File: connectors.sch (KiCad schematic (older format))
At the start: 29 parts, among them J10 Servo3, J11 Servo4, J12 Servo5, J13 CAN, J14 Servo6, J15 Servo7, J16 Servo8, J8 Servo1, J9 Servo2, U3 LP38693-5.0, U4 TXB0108DQSR, U5 MCP2551

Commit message: Final changes in schema
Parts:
- added C16: 10uF, symbol Device:CP
- C13: renamed from C15; value 100uF -> 10uF
- renumbered C16 to C14, C17 to C15, C18 to C17, C19 to C18, C20 to C19, C21 to C20, C22 to C21, C23 to C22, C24 to C23, C25 to C24, C26 to C25, C27 to C26, C28 to C27
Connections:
- net GND: now also C16.2
- net VCCOUT: now also C16.1
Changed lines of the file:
@@
 encoding utf-8
 Sheet 2 3
-Title ""
-Date ""
-Rev ""
-Comp ""
-Comment1 ""
+Title "SX1280 based RC receiver"
+Date "2019-02-25"
+Rev "1"
+Comp "bodrico.com"
+Comment1 "Designed by bodri@bodrico.com"
 Comment2 ""
 Comment3 ""
@@
 	8375 2150 8225 2150
 $Comp
-L Device:C C16
+L Device:C C14
 U 1 1 5C78CA1B
 P 6550 2250
-F 0 "C16" H 6665 2296 50  0000 L CNN
+F 0 "C14" H 6665 2296 50  0000 L CNN
 F 1 "1uF" H 6665 2205 50  0000 L CNN
 F 2 "" H 6588 2100 50  0001 C CNN
@@
 $EndComp
 $Comp
-L Device:C C17
+L Device:C C15
 U 1 1 5C78CA91
 P 8375 2300
-F 0 "C17" H 8490 2346 50  0000 L CNN
+F 0 "C15" H 8490 2346 50  0000 L CNN
 F 1 "1uF" H 8490 2255 50  0000 L CNN
 F 2 "" H 8413 2150 50  0001 C CNN
@@
 	7825 2500 7825 2450
 Wire Wire Line
-	8375 2050 8675 2050
+	8375 2050 8750 2050
 Connection ~ 8375 2050
-Text Label 8400 2050 0    50   ~ 0
+Text Label 8950 2050 0    50   ~ 0
 VCCOUT
 Wire Wire Line
@@
 	2925 3400 3200 3400
 $Comp
-L Device:CP C15
+L Device:CP C13
 U 1 1 5C79ED78
 P 6100 2250
-F 0 "C15" H 6218 2296 50  0000 L CNN
-F 1 "100uF" H 6218 2205 50  0000 L CNN
+F 0 "C13" H 6218 2296 50  0000 L CNN
+F 1 "10uF" H 6218 2205 50  0000 L CNN
 F 2 "" H 6138 2100 50  0001 C CNN
 F 3 "~" H 6100 2250 50  0001 C CNN
@@
 $EndComp
 $Comp
-L Device:C C20
+L Device:C C19
 U 1 1 5C7D119D
 P 3950 2900
-F 0 "C20" V 3698 2900 50  0000 C CNN
+F 0 "C19" V 3698 2900 50  0000 C CNN
 F 1 "100nF" V 3789 2900 50  0000 C CNN
 F 2 "" H 3988 2750 50  0001 C CNN
@@
 	4175 2900 4175 2950
 $Comp
-L Device:C C19
+L Device:C C18
 U 1 1 5C7D7B7F
 P 3300 2900
-F 0 "C19" V 3048 2900 50  0000 C CNN
+F 0 "C18" V 3048 2900 50  0000 C CNN
 F 1 "100nF" V 3139 2900 50  0000 C CNN
 F 2 "" H 3338 2750 50  0001 C CNN
@@
 P 7750 3850
 AR Path="/5CCDDFB0" Ref="C?"  Part="1"
-AR Path="/5C76B390/5CCDDFB0" Ref="C23"  Part="1"
-F 0 "C23" V 7498 3850 50  0000 C CNN
+AR Path="/5C76B390/5CCDDFB0" Ref="C22"  Part="1"
+F 0 "C22" V 7498 3850 50  0000 C CNN
 F 1 "100nF" V 7589 3850 50  0000 C CNN
 F 2 "" H 7788 3700 50  0001 C CNN
@@
 	9000 4500 9100 4500
 $Comp
-L Device:C C21
+L Device:C C20
 U 1 1 5CCE1675
 P 4700 2950
-F 0 "C21" H 4815 2996 50  0000 L CNN
+F 0 "C20" H 4815 2996 50  0000 L CNN
 F 1 "470pF" H 4815 2905 50  0000 L CNN
 F 2 "" H 4738 2800 50  0001 C CNN
@@
 $EndComp
 $Comp
-L Device:C C18
+L Device:C C17
 U 1 1 5CCE1727
 P 4700 2500
-F 0 "C18" H 4815 2546 50  0000 L CNN
+F 0 "C17" H 4815 2546 50  0000 L CNN
 F 1 "470pF" H 4815 2455 50  0000 L CNN
 F 2 "" H 4738 2350 50  0001 C CNN
@@
 	4700 2350 5250 2350
 $Comp
-L Device:C C28
+L Device:C C27
 U 1 1 5CCE1785
 P 4200 5700
-F 0 "C28" H 4315 5746 50  0000 L CNN
+F 0 "C27" H 4315 5746 50  0000 L CNN
 F 1 "470pF" H 4315 5655 50  0000 L CNN
 F 2 "" H 4238 5550 50  0001 C CNN
@@
 $EndComp
 $Comp
-L Device:C C27
+L Device:C C26
 U 1 1 5CCE1C56
 P 4350 5250
-F 0 "C27" H 4465 5296 50  0000 L CNN
+F 0 "C26" H 4465 5296 50  0000 L CNN
 F 1 "470pF" H 4465 5205 50  0000 L CNN
 F 2 "" H 4388 5100 50  0001 C CNN
@@
 $EndComp
 $Comp
-L Device:C C26
+L Device:C C25
 U 1 1 5CCE1CA6
 P 4500 4800
-F 0 "C26" H 4615 4846 50  0000 L CNN
+F 0 "C25" H 4615 4846 50  0000 L CNN
 F 1 "470pF" H 4615 4755 50  0000 L CNN
 F 2 "" H 4538 4650 50  0001 C CNN
@@
 $EndComp
 $Comp
-L Device:C C25
+L Device:C C24
 U 1 1 5CCE1CFA
 P 4650 4350
-F 0 "C25" H 4765 4396 50  0000 L CNN
+F 0 "C24" H 4765 4396 50  0000 L CNN
 F 1 "470pF" H 4765 4305 50  0000 L CNN
 F 2 "" H 4688 4200 50  0001 C CNN
@@
 Connection ~ 4650 4150
 $Comp
-L Device:C C24
+L Device:C C23
 U 1 1 5CD045AA
 P 4775 3925
-F 0 "C24" H 4800 4025 50  0000 L CNN
+F 0 "C23" H 4800 4025 50  0000 L CNN
 F 1 "470pF" H 4800 3825 50  0000 L CNN
 F 2 "" H 4813 3775 50  0001 C CNN
@@
 $EndComp
 $Comp
-L Device:C C22
+L Device:C C21
 U 1 1 5CD17DAF
 P 4700 3400
-F 0 "C22" H 4815 3446 50  0000 L CNN
+F 0 "C21" H 4815 3446 50  0000 L CNN
 F 1 "470pF" H 4815 3355 50  0000 L CNN
 F 2 "" H 4738 3250 50  0001 C CNN
@@
 Wire Wire Line
 	8200 4200 7925 4200
+$Comp
+L Device:CP C16
+U 1 1 5CE22492
+P 8750 2300
+F 0 "C16" H 8868 2346 50  0000 L CNN
+F 1 "10uF" H 8868 2255 50  0000 L CNN
+F 2 "" H 8788 2150 50  0001 C CNN
+F 3 "~" H 8750 2300 50  0001 C CNN
+	1    8750 2300
+	1    0    0    -1
+$EndComp
+Wire Wire Line
+	8750 2050 8750 2150
+Connection ~ 8750 2050
+Wire Wire Line
+	8750 2050 9250 2050
+Wire Wire Line
+	8375 2500 8750 2500
+Wire Wire Line
+	8750 2500 8750 2450
+Connection ~ 8375 2500
 $EndSCHEMATC

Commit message: Add some footprints
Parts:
- C13, C16: footprint (none) -> Capacitor_Tantalum_SMD:CP_EIA-3216-18_Kemet-A
- C14, C15, C17, C18, C19, C20, C21, C22, C23, C24, C25, C26, C27: footprint (none) -> Capacitor_SMD:C_0402_1005Metric
- J13: footprint (none) -> Connector_JST:JST_PH_B3B-PH-SM4-TB_1x03-1MP_P2.00mm_Vertical
- R7, R8, R9: footprint (none) -> Resistor_SMD:R_0402_1005Metric
- U3: footprint (none) -> miscellaneous:WSON-6_3x3mm_Pitch0.95mm
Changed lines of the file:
@@
 EESchema Schematic File Version 4
+LIBS:RcReceiver-cache
 EELAYER 26 0
 EELAYER END
@@
 F 0 "C14" H 6665 2296 50  0000 L CNN
 F 1 "1uF" H 6665 2205 50  0000 L CNN
-F 2 "" H 6588 2100 50  0001 C CNN
+F 2 "Capacitor_SMD:C_0402_1005Metric" H 6588 2100 50  0001 C CNN
 F 3 "~" H 6550 2250 50  0001 C CNN
 	1    6550 2250
@@
 F 0 "C15" H 8490 2346 50  0000 L CNN
 F 1 "1uF" H 8490 2255 50  0000 L CNN
-F 2 "" H 8413 2150 50  0001 C CNN
+F 2 "Capacitor_SMD:C_0402_1005Metric" H 8413 2150 50  0001 C CNN
 F 3 "~" H 8375 2300 50  0001 C CNN
 	1    8375 2300
@@
 F 0 "C13" H 6218 2296 50  0000 L CNN
 F 1 "10uF" H 6218 2205 50  0000 L CNN
-F 2 "" H 6138 2100 50  0001 C CNN
+F 2 "Capacitor_Tantalum_SMD:CP_EIA-3216-18_Kemet-A" H 6138 2100 50  0001 C CNN
 F 3 "~" H 6100 2250 50  0001 C CNN
 	1    6100 2250
@@
 F 0 "U3" H 7825 2515 50  0000 C CNN
 F 1 "LP38693-5.0" H 7825 2424 50  0000 C CNN
-F 2 "" H 7825 2150 50  0001 C CNN
+F 2 "miscellaneous:WSON-6_3x3mm_Pitch0.95mm" H 7825 2150 50  0001 C CNN
 F 3 "http://www.ti.com/lit/ds/snvs321o/snvs321o.pdf" H 7825 2150 50  0001 C CNN
 	1    7825 2150
@@
 F 0 "C19" V 3698 2900 50  0000 C CNN
 F 1 "100nF" V 3789 2900 50  0000 C CNN
-F 2 "" H 3988 2750 50  0001 C CNN
+F 2 "Capacitor_SMD:C_0402_1005Metric" H 3988 2750 50  0001 C CNN
 F 3 "~" H 3950 2900 50  0001 C CNN
 	1    3950 2900
@@
 F 0 "C18" V 3048 2900 50  0000 C CNN
 F 1 "100nF" V 3139 2900 50  0000 C CNN
-F 2 "" H 3338 2750 50  0001 C CNN
+F 2 "Capacitor_SMD:C_0402_1005Metric" H 3338 2750 50  0001 C CNN
 F 3 "~" H 3300 2900 50  0001 C CNN
 	1    3300 2900
@@
 F 0 "C22" V 7498 3850 50  0000 C CNN
 F 1 "100nF" V 7589 3850 50  0000 C CNN
-F 2 "" H 7788 3700 50  0001 C CNN
+F 2 "Capacitor_SMD:C_0402_1005Metric" H 7788 3700 50  0001 C CNN
 F 3 "~" H 7750 3850 50  0001 C CNN
 	1    7750 3850
@@
 F 0 "R8" H 8170 4746 50  0000 L CNN
 F 1 "4k7" H 8170 4655 50  0000 L CNN
-F 2 "" V 8030 4700 50  0001 C CNN
+F 2 "Resistor_SMD:R_0402_1005Metric" V 8030 4700 50  0001 C CNN
 F 3 "~" H 8100 4700 50  0001 C CNN
 	1    8100 4700
@@
 F 0 "R9" H 8445 4746 50  0000 L CNN
 F 1 "120R" H 8445 4655 50  0000 L CNN
-F 2 "" V 8305 4700 50  0001 C CNN
+F 2 "Resistor_SMD:R_0402_1005Metric" V 8305 4700 50  0001 C CNN
 F 3 "~" H 8375 4700 50  0001 C CNN
 	1    8375 4700
@@
 F 0 "J13" H 9380 4442 50  0000 L CNN
 F 1 "CAN" H 9380 4351 50  0000 L CNN
-F 2 "" H 9300 4400 50  0001 C CNN
+F 2 "Connector_JST:JST_PH_B3B-PH-SM4-TB_1x03-1MP_P2.00mm_Vertical" H 9300 4400 50  0001 C CNN
 F 3 "~" H 9300 4400 50  0001 C CNN
 	1    9300 4400
@@
 F 0 "C20" H 4815 2996 50  0000 L CNN
 F 1 "470pF" H 4815 2905 50  0000 L CNN
-F 2 "" H 4738 2800 50  0001 C CNN
+F 2 "Capacitor_SMD:C_0402_1005Metric" H 4738 2800 50  0001 C CNN
 F 3 "~" H 4700 2950 50  0001 C CNN
 	1    4700 2950
@@
 F 0 "C17" H 4815 2546 50  0000 L CNN
 F 1 "470pF" H 4815 2455 50  0000 L CNN
-F 2 "" H 4738 2350 50  0001 C CNN
+F 2 "Capacitor_SMD:C_0402_1005Metric" H 4738 2350 50  0001 C CNN
 F 3 "~" H 4700 2500 50  0001 C CNN
 	1    4700 2500
@@
 F 0 "C27" H 4315 5746 50  0000 L CNN
 F 1 "470pF" H 4315 5655 50  0000 L CNN
-F 2 "" H 4238 5550 50  0001 C CNN
+F 2 "Capacitor_SMD:C_0402_1005Metric" H 4238 5550 50  0001 C CNN
 F 3 "~" H 4200 5700 50  0001 C CNN
 	1    4200 5700
@@
 F 0 "C26" H 4465 5296 50  0000 L CNN
 F 1 "470pF" H 4465 5205 50  0000 L CNN
-F 2 "" H 4388 5100 50  0001 C CNN
+F 2 "Capacitor_SMD:C_0402_1005Metric" H 4388 5100 50  0001 C CNN
 F 3 "~" H 4350 5250 50  0001 C CNN
 	1    4350 5250
@@
 F 0 "C25" H 4615 4846 50  0000 L CNN
 F 1 "470pF" H 4615 4755 50  0000 L CNN
-F 2 "" H 4538 4650 50  0001 C CNN
+F 2 "Capacitor_SMD:C_0402_1005Metric" H 4538 4650 50  0001 C CNN
 F 3 "~" H 4500 4800 50  0001 C CNN
 	1    4500 4800
@@
 F 0 "C24" H 4765 4396 50  0000 L CNN
 F 1 "470pF" H 4765 4305 50  0000 L CNN
-F 2 "" H 4688 4200 50  0001 C CNN
+F 2 "Capacitor_SMD:C_0402_1005Metric" H 4688 4200 50  0001 C CNN
 F 3 "~" H 4650 4350 50  0001 C CNN
 	1    4650 4350
@@
 F 0 "C23" H 4800 4025 50  0000 L CNN
 F 1 "470pF" H 4800 3825 50  0000 L CNN
-F 2 "" H 4813 3775 50  0001 C CNN
+F 2 "Capacitor_SMD:C_0402_1005Metric" H 4813 3775 50  0001 C CNN
 F 3 "~" H 4775 3925 50  0001 C CNN
 	1    4775 3925
@@
 F 0 "C21" H 4815 3446 50  0000 L CNN
 F 1 "470pF" H 4815 3355 50  0000 L CNN
-F 2 "" H 4738 3250 50  0001 C CNN
+F 2 "Capacitor_SMD:C_0402_1005Metric" H 4738 3250 50  0001 C CNN
 F 3 "~" H 4700 3400 50  0001 C CNN
 	1    4700 3400
@@
 F 0 "R7" V 7100 2250 50  0000 C CNN
 F 1 "470k" V 7300 2250 50  0000 C CNN
-F 2 "" V 7130 2250 50  0001 C CNN
+F 2 "Resistor_SMD:R_0402_1005Metric" V 7130 2250 50  0001 C CNN
 F 3 "~" H 7200 2250 50  0001 C CNN
 	1    7200 2250
@@
 F 0 "C16" H 8868 2346 50  0000 L CNN
 F 1 "10uF" H 8868 2255 50  0000 L CNN
-F 2 "" H 8788 2150 50  0001 C CNN
+F 2 "Capacitor_Tantalum_SMD:CP_EIA-3216-18_Kemet-A" H 8788 2150 50  0001 C CNN
 F 3 "~" H 8750 2300 50  0001 C CNN
 	1    8750 2300

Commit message: Create PCB
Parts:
- J10, J11, J12, J14, J15, J16, J8, J9: footprint (none) -> miscellaneous:PinHeader_1x03_P1.27mm_Side
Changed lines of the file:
@@
 F 0 "J8" H 5530 2492 50  0000 L CNN
 F 1 "Servo1" H 5530 2401 50  0000 L CNN
-F 2 "" H 5450 2450 50  0001 C CNN
+F 2 "miscellaneous:PinHeader_1x03_P1.27mm_Side" H 5450 2450 50  0001 C CNN
 F 3 "~" H 5450 2450 50  0001 C CNN
 	1    5450 2450
@@
 F 0 "J9" H 5530 2942 50  0000 L CNN
 F 1 "Servo2" H 5530 2851 50  0000 L CNN
-F 2 "" H 5450 2900 50  0001 C CNN
+F 2 "miscellaneous:PinHeader_1x03_P1.27mm_Side" H 5450 2900 50  0001 C CNN
 F 3 "~" H 5450 2900 50  0001 C CNN
 	1    5450 2900
@@
 F 0 "J10" H 5530 3392 50  0000 L CNN
 F 1 "Servo3" H 5530 3301 50  0000 L CNN
-F 2 "" H 5450 3350 50  0001 C CNN
+F 2 "miscellaneous:PinHeader_1x03_P1.27mm_Side" H 5450 3350 50  0001 C CNN
 F 3 "~" H 5450 3350 50  0001 C CNN
 	1    5450 3350
@@
 F 0 "J11" H 5530 3842 50  0000 L CNN
 F 1 "Servo4" H 5530 3751 50  0000 L CNN
-F 2 "" H 5450 3800 50  0001 C CNN
+F 2 "miscellaneous:PinHeader_1x03_P1.27mm_Side" H 5450 3800 50  0001 C CNN
 F 3 "~" H 5450 3800 50  0001 C CNN
 	1    5450 3800
@@
 F 0 "J12" H 5530 4292 50  0000 L CNN
 F 1 "Servo5" H 5530 4201 50  0000 L CNN
-F 2 "" H 5450 4250 50  0001 C CNN
+F 2 "miscellaneous:PinHeader_1x03_P1.27mm_Side" H 5450 4250 50  0001 C CNN
 F 3 "~" H 5450 4250 50  0001 C CNN
 	1    5450 4250
@@
 F 0 "J14" H 5530 4742 50  0000 L CNN
 F 1 "Servo6" H 5530 4651 50  0000 L CNN
-F 2 "" H 5450 4700 50  0001 C CNN
+F 2 "miscellaneous:PinHeader_1x03_P1.27mm_Side" H 5450 4700 50  0001 C CNN
 F 3 "~" H 5450 4700 50  0001 C CNN
 	1    5450 4700
@@
 F 0 "J15" H 5530 5192 50  0000 L CNN
 F 1 "Servo7" H 5530 5101 50  0000 L CNN
-F 2 "" H 5450 5150 50  0001 C CNN
+F 2 "miscellaneous:PinHeader_1x03_P1.27mm_Side" H 5450 5150 50  0001 C CNN
 F 3 "~" H 5450 5150 50  0001 C CNN
 	1    5450 5150
@@
 F 0 "J16" H 5530 5642 50  0000 L CNN
 F 1 "Servo8" H 5530 5551 50  0000 L CNN
-F 2 "" H 5450 5600 50  0001 C CNN
+F 2 "miscellaneous:PinHeader_1x03_P1.27mm_Side" H 5450 5600 50  0001 C CNN
 F 3 "~" H 5450 5600 50  0001 C CNN
 	1    5450 5600
@@
 	8750 2500 8750 2450
 Connection ~ 8375 2500
+Text Label 5000 2050 2    50   ~ 0
+VCC
 $EndSCHEMATC

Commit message: Place all the components on the board
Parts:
- added J17: GND for the Servo connectors, Connector_PinHeader_2.54mm:PinHeader_1x01_P2.54mm_Vertical, symbol Connector_Generic:Conn_01x01
- J13: footprint Connector_JST:JST_PH_B3B-PH-SM4-TB_1x03-1MP_P2.00mm_Vertical -> Connector_JST:JST_SH_BM03B-SRSS-TB_1x03-1MP_P1.00mm_Vertical
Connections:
- net GND: now also J17.1 (Pin_1)
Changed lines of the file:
@@
 F 0 "J13" H 9380 4442 50  0000 L CNN
 F 1 "CAN" H 9380 4351 50  0000 L CNN
-F 2 "Connector_JST:JST_PH_B3B-PH-SM4-TB_1x03-1MP_P2.00mm_Vertical" H 9300 4400 50  0001 C CNN
+F 2 "Connector_JST:JST_SH_BM03B-SRSS-TB_1x03-1MP_P1.00mm_Vertical" H 9300 4400 50  0001 C CNN
 F 3 "~" H 9300 4400 50  0001 C CNN
 	1    9300 4400
@@
 Text Label 5000 2050 2    50   ~ 0
 VCC
+$Comp
+L Connector_Generic:Conn_01x01 J17
+U 1 1 5CF3538C
+P 5450 6350
+F 0 "J17" H 5529 6392 50  0000 L CNN
+F 1 "GND for the Servo connectors" H 5529 6301 50  0000 L CNN
+F 2 "Connector_PinHeader_2.54mm:PinHeader_1x01_P2.54mm_Vertical" H 5450 6350 50  0001 C CNN
+F 3 "~" H 5450 6350 50  0001 C CNN
+	1    5450 6350
+	1    0    0    -1
+$EndComp
+$Comp
+L power:GND #PWR031
+U 1 1 5CF35494
+P 5200 6400
+F 0 "#PWR031" H 5200 6150 50  0001 C CNN
+F 1 "GND" H 5205 6227 50  0000 C CNN
+F 2 "" H 5200 6400 50  0001 C CNN
+F 3 "" H 5200 6400 50  0001 C CNN
+	1    5200 6400
+	1    0    0    -1
+$EndComp
+Wire Wire Line
+	5200 6400 5200 6350
+Wire Wire Line
+	5200 6350 5250 6350
 $EndSCHEMATC

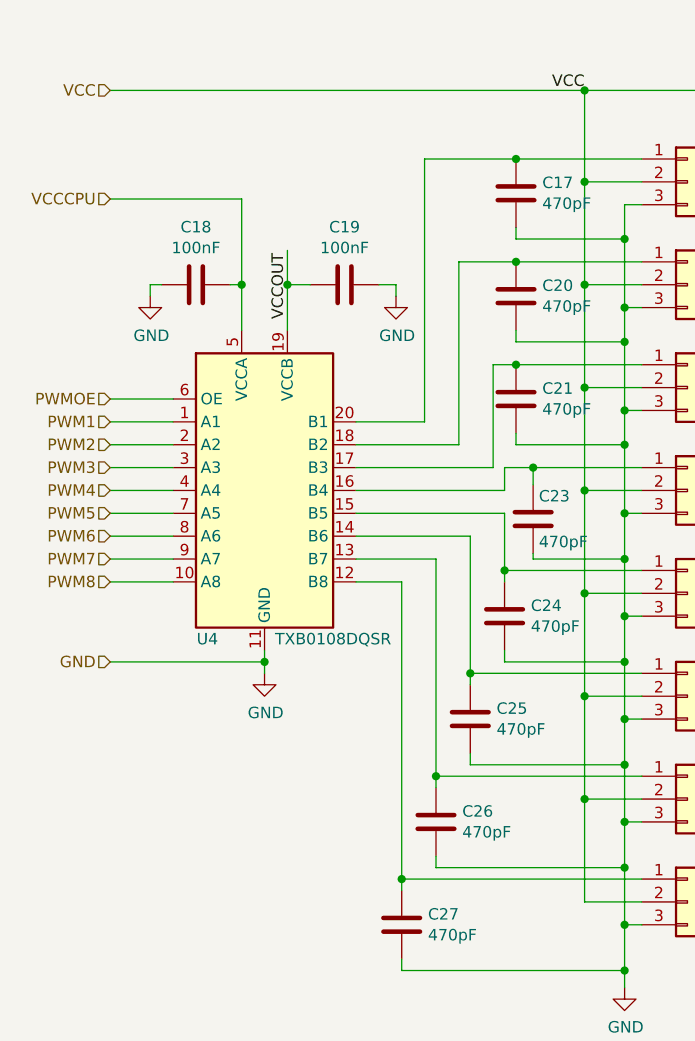
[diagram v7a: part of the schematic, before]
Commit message: Change TBX0108 footprint
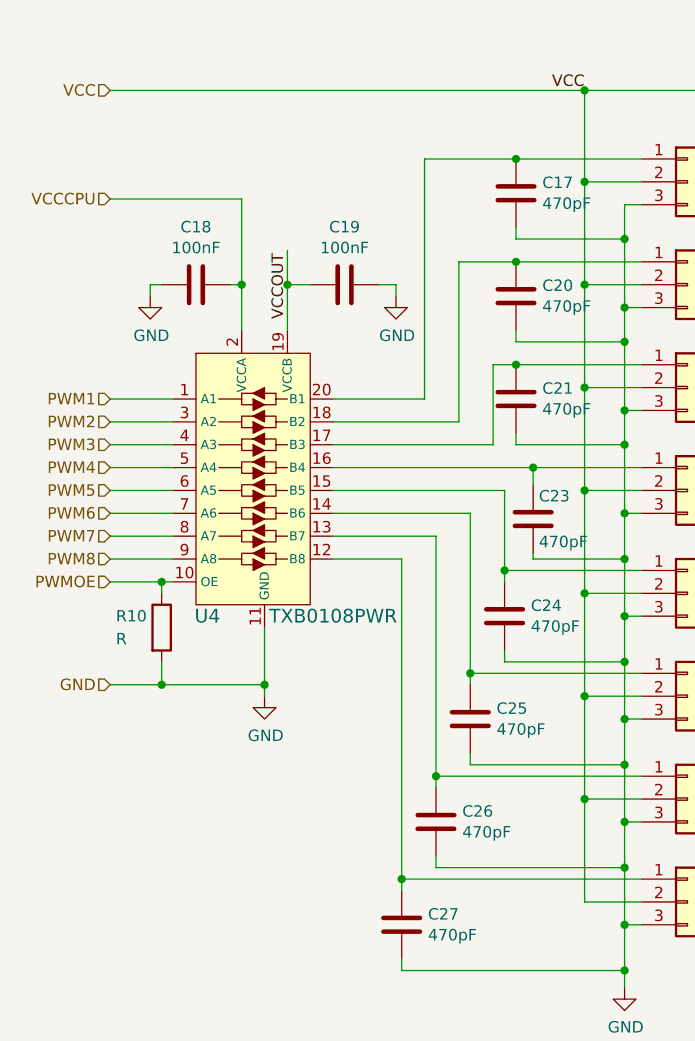
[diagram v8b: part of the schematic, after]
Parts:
- removed U4: TXB0108DQSR, Package_SON:USON-20_2x4mm_P0.4mm, symbol Logic_LevelTranslator:TXB0108DQSR
- added R10: R, Resistor_SMD:R_0402_1005Metric, symbol Device:R
- added U4: TXB0108PWR, digikey-footprints:TSSOP-20_W4.4mm, symbol dk_Logic-Translators-Level-Shifters:TXB0108PWR
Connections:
- net GND: now also R10.2, U4.11 (GND)
- net PWM1: now also U4.1 (A1)
- net PWM2: now also U4.3 (A2)
- net PWM3: now also U4.4 (A3)
- net PWM4: now also U4.5 (A4)
- net PWM5: now also U4.6 (A5)
- net PWM6: now also U4.7 (A6)
- net PWM7: now also U4.8 (A7)
- net PWM8: now also U4.9 (A8)
- net PWMOE: now also R10.1, U4.10 (OE)
- net VCCCPU: now also U4.2 (VCCA)
- net VCCOUT: now also U4.19 (VCCB)
- net at C17.1, J8.1 (Pin_1): now also U4.20 (B1)
- net at C20.1, J9.1 (Pin_1): now also U4.18 (B2)
- net at C21.1, J10.1 (Pin_1): now also U4.17 (B3)
- net at C23.1, J11.1 (Pin_1): now also U4.16 (B4)
- net at C24.1, J12.1 (Pin_1): now also U4.15 (B5)
- net at C25.1, J14.1 (Pin_1): now also U4.14 (B6)
- net at C26.1, J15.1 (Pin_1): now also U4.13 (B7)
- net at C27.1, J16.1 (Pin_1): now also U4.12 (B8)
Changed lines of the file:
@@
 	1    0    0    -1
 $EndComp
-$Comp
-L Logic_LevelTranslator:TXB0108DQSR U4
-U 1 1 5C76B772
-P 3600 3800
-F 0 "U4" H 3350 3150 50  0000 C CNN
-F 1 "TXB0108DQSR" H 3900 3150 50  0000 C CNN
-F 2 "Package_SON:USON-20_2x4mm_P0.4mm" H 3600 3050 50  0001 C CNN
-F 3 "http://www.ti.com/lit/ds/symlink/txb0108.pdf" H 3600 3700 50  0001 C CNN
-	1    3600 3800
-	1    0    0    -1
-$EndComp
-Wire Wire Line
-	4000 3500 4300 3500
-Wire Wire Line
-	4300 3500 4300 2350
+Wire Wire Line
+	3900 3400 4300 3400
+Wire Wire Line
+	4300 3400 4300 2350
 Wire Wire Line
 	4300 2350 4700 2350
 Wire Wire Line
-	4000 3600 4450 3600
-Wire Wire Line
-	4450 3600 4450 2800
+	3900 3500 4450 3500
+Wire Wire Line
+	4450 3500 4450 2800
 Wire Wire Line
 	4450 2800 4700 2800
 Wire Wire Line
-	4000 3700 4600 3700
-Wire Wire Line
-	4600 3700 4600 3250
+	3900 3600 4600 3600
+Wire Wire Line
+	4600 3600 4600 3250
 Wire Wire Line
 	4600 3250 4700 3250
 Wire Wire Line
-	4000 3800 4650 3800
-Wire Wire Line
-	4650 3800 4650 3700
-Wire Wire Line
-	4650 3700 4775 3700
-Wire Wire Line
-	4000 3900 4650 3900
-Wire Wire Line
-	4650 3900 4650 4150
+	3900 3800 4650 3800
+Wire Wire Line
+	4650 3800 4650 4150
 Wire Wire Line
 	4650 4150 5250 4150
 Wire Wire Line
-	4000 4000 4500 4000
-Wire Wire Line
-	4500 4000 4500 4600
+	3900 3900 4500 3900
+Wire Wire Line
+	4500 3900 4500 4600
 Wire Wire Line
 	4500 4600 5250 4600
 Wire Wire Line
-	4000 4100 4350 4100
-Wire Wire Line
-	4350 4100 4350 5050
+	3900 4000 4350 4000
+Wire Wire Line
+	4350 4000 4350 5050
 Wire Wire Line
 	4350 5050 5250 5050
 Wire Wire Line
-	4000 4200 4200 4200
-Wire Wire Line
-	4200 4200 4200 5500
+	3900 4100 4200 4100
+Wire Wire Line
+	4200 4100 4200 5500
 Wire Wire Line
 	4200 5500 5250 5500
 Text HLabel 2925 3500 0    50   Input ~ 0
-PWM1
+PWM2
 Text HLabel 2925 3600 0    50   Input ~ 0
-PWM2
+PWM3
 Text HLabel 2925 3700 0    50   Input ~ 0
-PWM3
+PWM4
 Text HLabel 2925 3800 0    50   Input ~ 0
-PWM4
+PWM5
 Text HLabel 2925 3900 0    50   Input ~ 0
-PWM5
+PWM6
 Text HLabel 2925 4000 0    50   Input ~ 0
-PWM6
+PWM7
 Text HLabel 2925 4100 0    50   Input ~ 0
-PWM7
+PWM8
 Text HLabel 2925 4200 0    50   Input ~ 0
-PWM8
+PWMOE
 Wire Wire Line
 	2925 3500 3200 3500
@@
 	2925 4100 3200 4100
 Wire Wire Line
-	2925 4200 3200 4200
+	2925 4200 3150 4200
 $Comp
 L power:GND #PWR022
 U 1 1 5C7744C7
-P 3600 4600
-F 0 "#PWR022" H 3600 4350 50  0001 C CNN
-F 1 "GND" H 3605 4427 50  0000 C CNN
-F 2 "" H 3600 4600 50  0001 C CNN
-F 3 "" H 3600 4600 50  0001 C CNN
-	1    3600 4600
-	1    0    0    -1
-$EndComp
-Wire Wire Line
-	3600 4600 3600 4550
+P 3600 4700
+F 0 "#PWR022" H 3600 4450 50  0001 C CNN
+F 1 "GND" H 3605 4527 50  0000 C CNN
+F 2 "" H 3600 4700 50  0001 C CNN
+F 3 "" H 3600 4700 50  0001 C CNN
+	1    3600 4700
+	1    0    0    -1
+$EndComp
+Wire Wire Line
+	3600 4700 3600 4650
 $Comp
 L power:GND #PWR024
@@
 	2925 2050 5000 2050
 Text HLabel 2925 3400 0    50   Input ~ 0
-PWMOE
-Text HLabel 2925 4550 0    50   Input ~ 0
+PWM1
+Text HLabel 2925 4650 0    50   Input ~ 0
 GND
-Wire Wire Line
-	2925 4550 3600 4550
-Connection ~ 3600 4550
-Wire Wire Line
-	3600 4550 3600 4500
+Connection ~ 3600 4650
 Wire Wire Line
 	2925 3400 3200 3400
@@
 Wire Wire Line
 	5200 6350 5250 6350
+$Comp
+L dk_Logic-Translators-Level-Shifters:TXB0108PWR U4
+U 1 1 5CB75ACC
+P 3600 3700
+F 0 "U4" H 3350 3050 60  0000 C CNN
+F 1 "TXB0108PWR" H 3900 3050 60  0000 C CNN
+F 2 "digikey-footprints:TSSOP-20_W4.4mm" H 3800 3900 60  0001 L CNN
+F 3 "http://www.ti.com/lit/ds/symlink/txb0108.pdf" H 3800 4000 60  0001 L CNN
+F 4 "296-21527-1-ND" H 3800 4100 60  0001 L CNN "Digi-Key_PN"
+F 5 "TXB0108PWR" H 3800 4200 60  0001 L CNN "MPN"
+F 6 "Integrated Circuits (ICs)" H 3800 4300 60  0001 L CNN "Category"
+F 7 "Logic - Translators, Level Shifters" H 3800 4400 60  0001 L CNN "Family"
+F 8 "http://www.ti.com/lit/ds/symlink/txb0108.pdf" H 3800 4500 60  0001 L CNN "DK_Datasheet_Link"
+F 9 "/product-detail/en/texas-instruments/TXB0108PWR/296-21527-1-ND/1305700" H 3800 4600 60  0001 L CNN "DK_Detail_Page"
+F 10 "IC TRNSLTR BIDIRECTIONAL 20TSSOP" H 3800 4700 60  0001 L CNN "Description"
+F 11 "Texas Instruments" H 3800 4800 60  0001 L CNN "Manufacturer"
+F 12 "Active" H 3800 4900 60  0001 L CNN "Status"
+	1    3600 3700
+	1    0    0    -1
+$EndComp
+Wire Wire Line
+	3900 3700 4775 3700
+$Comp
+L Device:R R10
+U 1 1 5CBE1CAD
+P 3150 4400
+F 0 "R10" H 2950 4450 50  0000 L CNN
+F 1 "R" H 2950 4350 50  0000 L CNN
+F 2 "Resistor_SMD:R_0402_1005Metric" V 3080 4400 50  0001 C CNN
+F 3 "~" H 3150 4400 50  0001 C CNN
+	1    3150 4400
+	1    0    0    -1
+$EndComp
+Wire Wire Line
+	3150 4250 3150 4200
+Connection ~ 3150 4200
+Wire Wire Line
+	3150 4200 3200 4200
+Wire Wire Line
+	3150 4550 3150 4650
+Wire Wire Line
+	2925 4650 3150 4650
+Connection ~ 3150 4650
+Wire Wire Line
+	3150 4650 3600 4650
+Wire Wire Line
+	3600 4400 3600 4650
 $EndSCHEMATC
